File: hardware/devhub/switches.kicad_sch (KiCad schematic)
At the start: 18 parts, among them U4 TPS2561ADRC, U5 TPS2561ADRC, U6 TPS2561ADRC, U7 INA3221, U8 INA3221

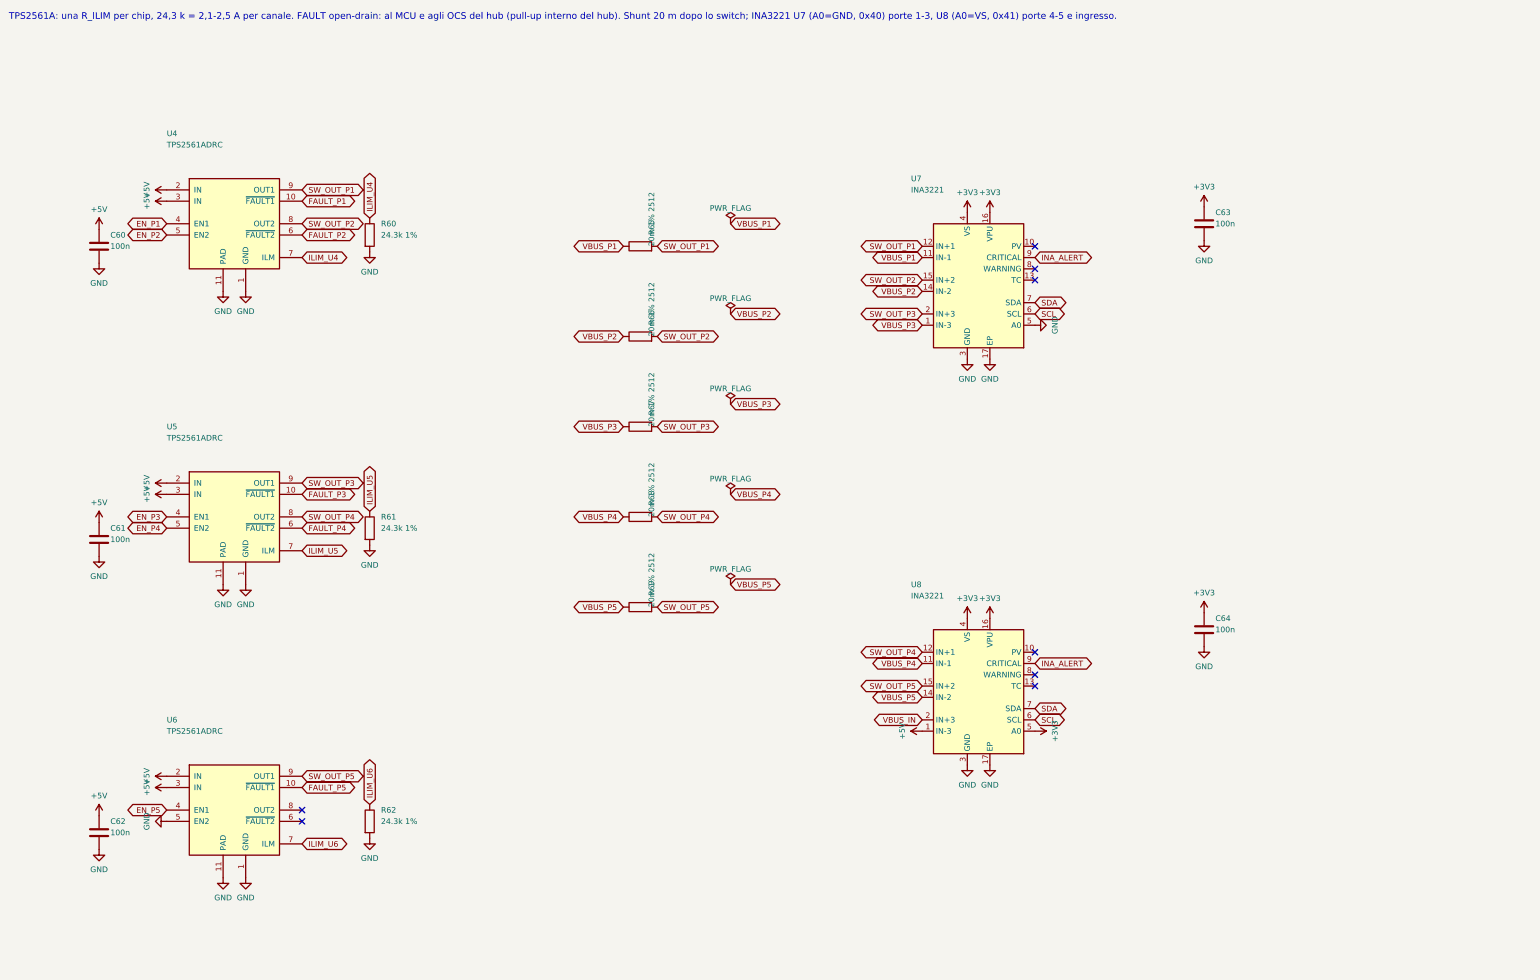
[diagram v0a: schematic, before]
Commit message: Schematic v0.2: hub reset supervisor, 1 A LDO, reorganized sheets, USB connectors and crystal
Functional changes:
- USB2517 RESET_N with pull-up and MCP120T-300 supervisor, wired-OR with
  the MCU (open-drain): resetting the MCU no longer resets the hub, so the
  ST DFU bootloader is reachable through it (D16/D17).
- 3.3 V LDO: AP7361C-33E (1 A, SOT-223) instead of AP2112K, which
  dissipated too much with the hub load.
- 74HC595 /OE on PB6 with pull-up: LEDs off until firmware enables them.
- Orange D93 instead of blue, USB-A bulk capacitance >= 120 uF, relay coil
  pinout fixed, snubbers marked DNP, Cliff FCR7350 banana jack footprints.
- D18: horizontal USB connectors, GCT USB4105-GF-A (USB-C) and Kycon
  KUSBX-AS1N-B (USB-A).
- D19: YXC X322524MOB4SI 24 MHz crystal (C_L 12 pF), 15 pF C0G load caps.

Layout: nearby parts wired directly, every net still explicitly named;
local labels inside sheets, global only across sheets, hierarchical for
ports. Files saved with KiCad 10.

Connectivity checked against the previous netlist, ERC clean.
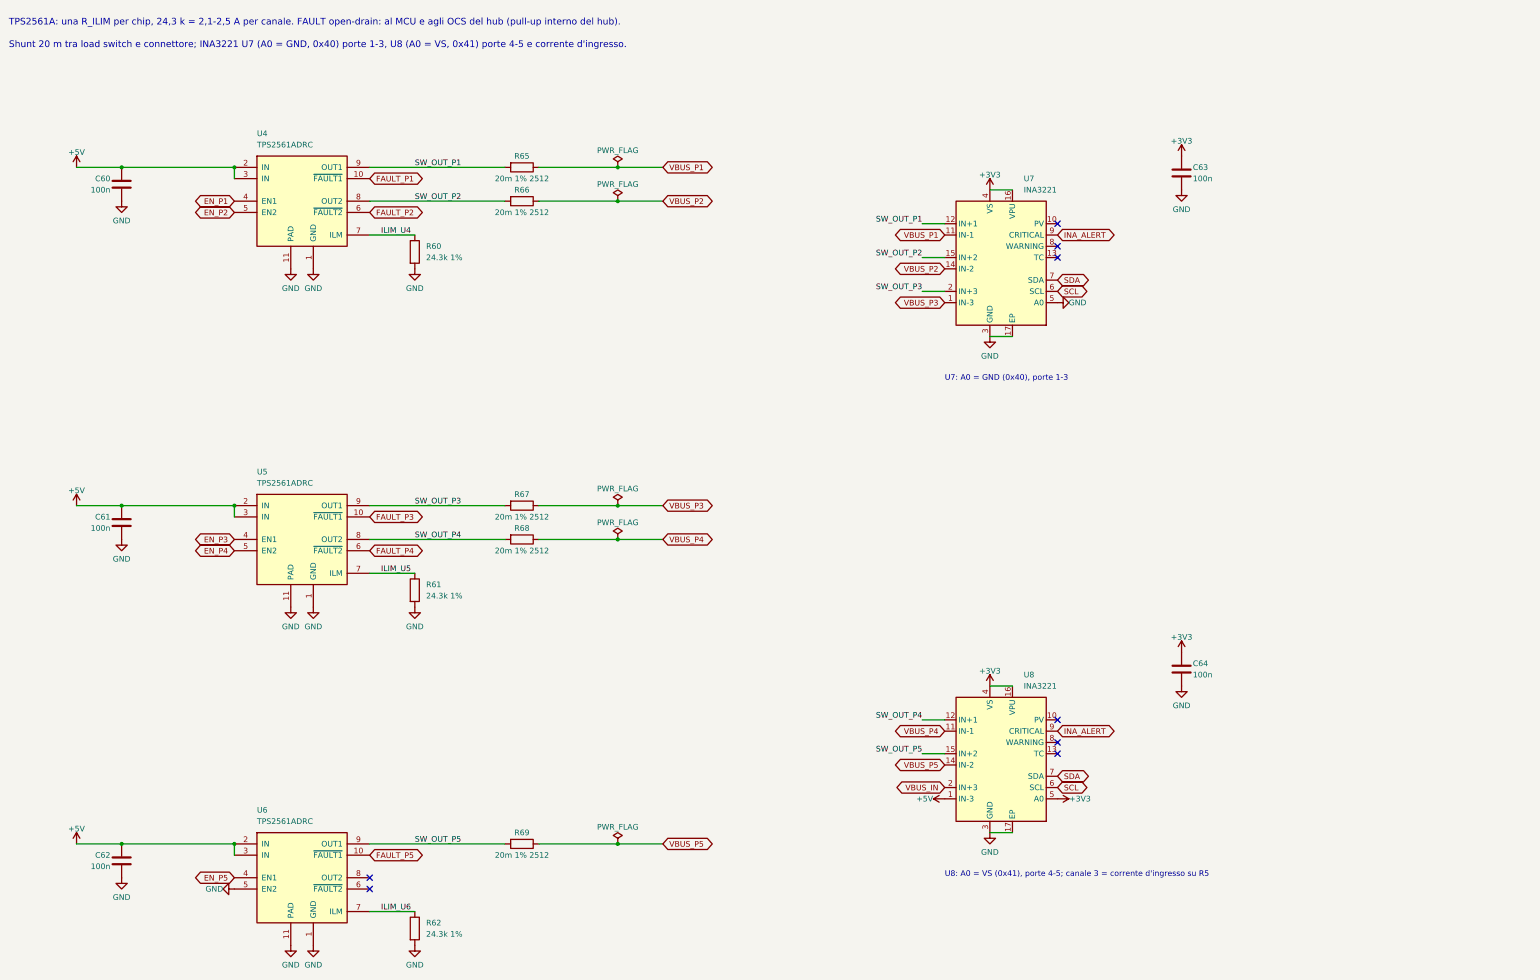
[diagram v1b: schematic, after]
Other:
- note added: "Shunt 20 m tra load switch e connettore; INA3221 U7 (A0 = GND, 0x40) porte 1-3, U8 (A0 = VS, 0x41) porte 4-5 e corrente d'ingresso."
- note added: "TPS2561A: una R_ILIM per chip, 24,3 k = 2,1-2,5 A per canale. FAULT open-drain: al MCU e agli OCS del hub (pull-up interno del hub)."
- note added: "U7: A0 = GND (0x40), porte 1-3"
- note added: "U8: A0 = VS (0x41), porte 4-5; canale 3 = corrente d'ingresso su R5"
- note removed: "TPS2561A: una R_ILIM per chip, 24,3 k = 2,1-2,5 A per canale. FAULT open-drain: al MCU e agli OCS del hub (pull-up interno del hub). Shunt 20 m dopo lo switch; INA3221 U7 (A0=GND, 0x40) porte 1-3, U8 (A0=VS, 0x41) porte 4-5 e ingresso."

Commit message: Lab-use protection: TPS259470A input eFuse, PI3USB4002A data switches; AGENTS.md
Power input (D20, D21):
- TPS259470A eFuse after the shunt: trips above 5.84 V and below 4.0 V,
  zener on EN to withstand up to 28 V, 3.5 A limit, ~5 ms soft start,
  auto-retry, FLT to the MCU on PB1.
- The shunt stays before the eFuse, so the INA3221 still measures the input
  voltage when the eFuse is off.

Ports (D22): PI3USB4002A instead of TS3USB30E. The connector side withstands
24 V and opens above 4.75 V, so a D+/D- short to VBUS on a board under test
no longer reaches the 3.3 V rail.

Symbols for both ICs added to the project library. AGENTS.md added: the
schematic is edited in KiCad or with targeted changes, never regenerated by
script. Sheets re-saved by KiCad.

Connectivity checked against the previous netlist, ERC clean.
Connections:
- net +5V: no longer U8.1 (IN-3)
- new net VIN_FUSE: U8.1 (IN-3)
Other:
- note added: "U8: A0 = VS (0x41), porte 4-5; canale 3 = corrente e tensione d'ingresso su R5"
- note removed: "U8: A0 = VS (0x41), porte 4-5; canale 3 = corrente d'ingresso su R5"

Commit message: Simplification: input shunt moved after the eFuse, VSYS_ADC divider removed (D40)
The INA3221 is no longer exposed to the supply voltage and reads 5V_SYS; LOCAL_PWR gets a 10k pull-up (R26). Push-button capacitors kept (D39).
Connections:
- net VIN_FUSE is gone; now on net +5V: U8.1 (IN-3)
- net VBUS_IN renamed 5V_EFUSE
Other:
- note added: "U8: A0 = VS (0x41), porte 4-5; canale 3 = corrente totale e 5V_SYS su R5 (dopo l'eFuse)"
- note removed: "U8: A0 = VS (0x41), porte 4-5; canale 3 = corrente e tensione d'ingresso su R5"
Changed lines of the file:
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@@
 		)
 	)
-	(text "U8: A0 = VS (0x41), porte 4-5; canale 3 = corrente e tensione d'ingresso su R5"
+	(text "U8: A0 = VS (0x41), porte 4-5; canale 3 = corrente totale e 5V_SYS su R5 (dopo l'eFuse)"
 		(exclude_from_sim no)
 		(at 220.98 208.28 0)
@@
 		)
 	)
-	(global_label "VIN_FUSE"
-		(shape bidirectional)
-		(at 220.98 190.5 180)
-		(fields_autoplaced yes)
-		(effects
-			(font
-				(size 1.27 1.27)
-			)
-			(justify right)
-		)
-		(property "Intersheetrefs" "${INTERSHEET_REFS}"
-			(at 220.98 190.5 0)
-			(hide yes)
-			(show_name no)
-			(do_not_autoplace no)
-			(effects
-				(font
-					(size 1.27 1.27)
-				)
-			)
-		)
-	)
 	(global_label "SDA"
 		(shape bidirectional)
@@
 		)
 	)
-	(global_label "VBUS_IN"
+	(global_label "5V_EFUSE"
 		(shape bidirectional)
 		(at 220.98 187.96 180)
@@
 					(unit 1)
 				)
+			)
+		)
+	)
+	(symbol
+		(lib_id "power:+5V")
+		(at 220.98 190.5 90)
+		(unit 1)
+		(body_style 1)
+		(exclude_from_sim no)
+		(in_bom yes)
+		(on_board yes)
+		(in_pos_files yes)
+		(dnp no)
+		(property "Reference" "#PWR160"
+			(at 220.98 190.5 0)
+			(hide yes)
+			(show_name no)
+			(do_not_autoplace no)
+			(effects
+				(font
+					(size 1.27 1.27)
+				)
+			)
+		)
+		(property "Value" "+5V"
+			(at 215.921 190.5 90)
+			(show_name no)
+			(do_not_autoplace no)
+			(effects
+				(font
+					(size 1.27 1.27)
+				)
+			)
+		)
+		(property "Footprint" ""
+			(at 220.98 190.5 0)
+			(hide yes)
+			(show_name no)
+			(do_not_autoplace no)
+			(effects
+				(font
+					(size 1.27 1.27)
+				)
+			)
+		)
+		(property "Datasheet" ""
+			(at 220.98 190.5 0)
+			(hide yes)
+			(show_name no)
+			(do_not_autoplace no)
+			(effects
+				(font
+					(size 1.27 1.27)
+				)
+			)
+		)
+		(property "Description" ""
+			(at 220.98 190.5 0)
+			(hide yes)
+			(show_name no)
+			(do_not_autoplace no)
+			(effects
+				(font
+					(size 1.27 1.27)
+				)
+			)
+		)
+		(pin "1"
+		)
+		(instances
+			(project "devhub"
+				(path "/af6ea7d8-d1ba-5fc6-aec8-abf514847630/1e0a4864-e5d3-5f33-ba41-65dd2f29348f"
+					(reference "#PWR160")
+					(unit 1)
+				)

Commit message: PCB rules in KiCad, USB pair names, eFuse output bypass and U2 thermal vias (D44-D50)
Stackup JLC04161H-7628, netclasses and custom DRC rules (devhub.kicad_dru) from
docs/regole-pcb.md, with a section for the checks that DRC cannot cover. C7 1 uF on
the TPS259470A output before the shunt (D48). USB nets renamed to DP/DN so KiCad
recognizes the differential pairs (D49). U2 footprint with 0.3 mm thermal vias, open
on both sides for the prototype; encroached vias and a JLCPCB order note for
production (D50). Also includes stock part codes, cost comparison and placement rules
(D44-D47).
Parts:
- C60, C61, C62, C63, C64: digikey (none) -> 1276-1000-1-ND; lcsc (none) -> C1591; mouser (none) -> 187-CL10B104KB8NNNC; warehouse (none) -> 235
- R60, R61, R62: digikey (none) -> 311-24.3KHRCT-ND; lcsc (none) -> C276290; mouser (none) -> 603-RC0603FR-0724K3L
- R65, R66, R67, R68, R69: digikey (none) -> 311-0.02TCT-ND; lcsc (none) -> C326611; mouser (none) -> 603-RL2512FK-070R02L
- U4, U5, U6: digikey (none) -> 296-43616-1-ND; lcsc (none) -> C473357; mouser (none) -> 595-TPS2561ADRCR
- U7, U8: digikey (none) -> 296-INA3221AIRGVRCT-ND; lcsc (none) -> C181255; mouser (none) -> 595-INA3221AIRGVR

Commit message: Review 03 fixes and PCB placement update (D51-D56)
Schematic review 03 (docs/lavorazioni/review_03.md):
- D1 SMAJ20A was reversed (cathode on GND): rotated, and replaced by a project
  symbol devhub:SMAJ20A with explicit K/A pin names; breakdown corrected to
  22.2-24.5 V (R03-01).
- D21 BAT54WS from VBUS_DET to 3V3 keeps USB2517 pin 44 within VDD33 + 0.5 V
  when the hub is unpowered (D53, R03-02).
- USB-A port limited to 1.5 A, the J501 connector rating: R62 33.2k, RF-5
  updated (D54, R03-03).
- RF-6 accuracy relaxed to 2 mA + 5 % because of the thick-film shunt TCR
  (D55, R03-04).
- Courtyards of the LCSC U13 and PI3USB4002A footprints enlarged to cover the
  pads, also in the PCB copies (R03-05).
- LDO U1 kept (buck rejected); GND heatsink zone and 10 vias on its tab, thermal
  budget corrected to 0.8-0.9 W worst case (D56).

PCB: connector layout (D51), USB pair polarity on the bottom side (D52), relays
moved with the contact keepout areas redrawn, D21 placed next to C21. Cost
comparison updated with D21 and R62.
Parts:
- R62: value 24.3k 1% -> 33.2k 1%; digikey 311-24.3KHRCT-ND -> 311-33.2KHRCT-ND; lcsc C276290 -> C185338; mouser 603-RC0603FR-0724K3L -> 603-RC0603FR-0733K2L
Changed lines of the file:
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@@
 			)
 		)
-		(property "Value" "24.3k 1%"
+		(property "Value" "33.2k 1%"
 			(at 104.14 220.98 0)
 			(show_name no)
@@
 			)
 		)
-		(property "lcsc" "C276290"
+		(property "lcsc" "C185338"
 			(at 101.6 219.71 0)
 			(hide yes)
@@
 			)
 		)
-		(property "mouser" "603-RC0603FR-0724K3L"
+		(property "mouser" "603-RC0603FR-0733K2L"
 			(at 101.6 219.71 0)
 			(hide yes)
@@
 			)
 		)
-		(property "digikey" "311-24.3KHRCT-ND"
+		(property "digikey" "311-33.2KHRCT-ND"
 			(at 101.6 219.71 0)
 			(hide yes)
